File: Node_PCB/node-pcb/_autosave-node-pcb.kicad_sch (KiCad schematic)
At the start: 37 parts, among them J1 TYPE-C-31-M-12, J2 TSW-102-07-G-S, J3 TSW-118-07-L-D, J4 TSW-118-07-L-D, U1 NCP1117ST33T3G, U3 RP2040, U4 W25Q32JVSSIQ, X1 12MHz

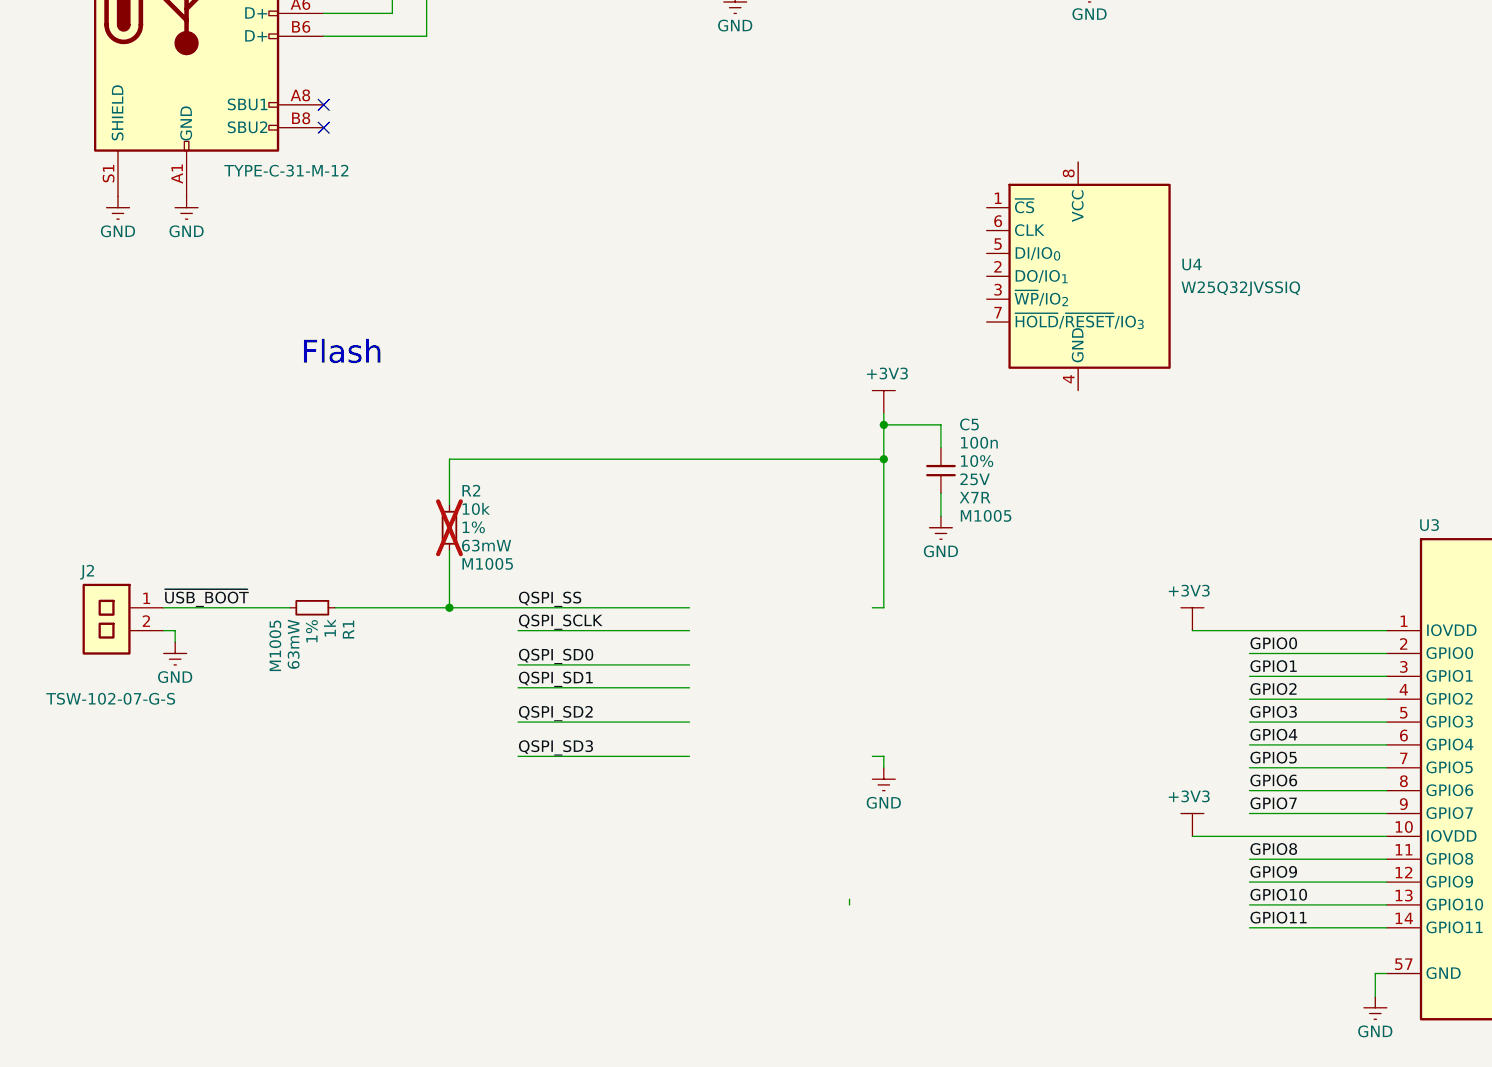
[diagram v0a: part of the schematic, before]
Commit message: Add new images for documentation and update existing schematic
- Added minimal example flash image to the documentation.
- Added schematic flash image to the documentation.
- Updated existing schematic power image.
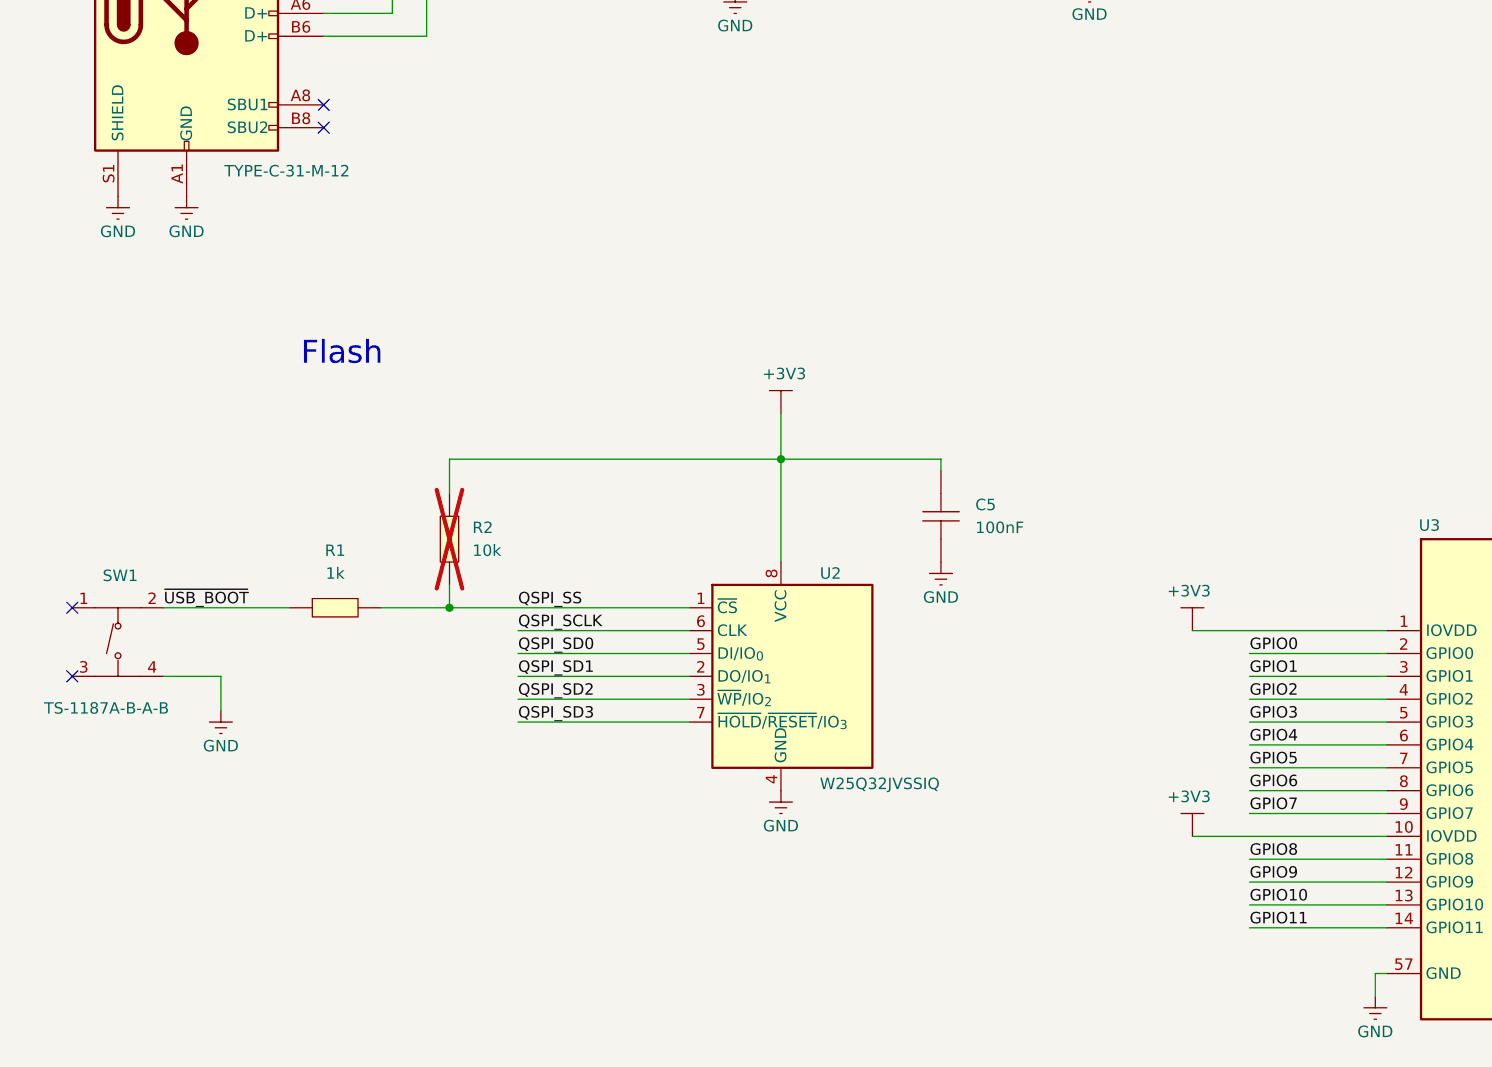
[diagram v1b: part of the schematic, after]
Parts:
- removed C5: 100n, RPI_COMPILED:generic_capc1005x50, symbol RPI_DB:Capacitors | MLCC | M1005/RP-01BJ9Y-KRGF41
- removed J2: TSW-102-07-G-S, RPI_COMPILED:samtec_tsw-102-07-g-s, symbol RPI_DB:Connectors | Pin_Headers/RP-01JV5X-LY21H5
- removed R1: 1k, RPI_COMPILED:generic_resc1005x35, symbol RPI_DB:Resistors | Chip | M1005/RP-019A1P-4Z6ZWY
- removed R2: 10k, RPI_COMPILED:generic_resc1005x35, symbol RPI_DB:Resistors | Chip | M1005/RP-019A1P-53DHSX
- added C5: 100nF, EasyEDA:C0402, symbol EasyEDA:CL05B104KO5NNNC
- added R1: 1k, EasyEDA:R0402, symbol EasyEDA:0402WGF1001TCE
- added R2: 10k, EasyEDA:R0402, symbol EasyEDA:0402WGF1002TCE
- added SW1: TS-1187A-B-A-B, EasyEDA:SW-SMD_4P-L5.1-W5.1-P3.70-LS6.5-TL_H1.5, symbol EasyEDA:TS-1187A-B-A-B
- renumbered U4 to U2
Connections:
- net +3V3: now also U2.8 (VCC), C5.1, R2.1
- net GND: now also U2.4 (GND), C5.2, SW1.4 (D)
- net QSPI_SCLK: now also U2.6 (CLK)
- net QSPI_SD0: now also U2.5 (DI/IO_{0})
- net QSPI_SD1: now also U2.2 (DO/IO_{1})
- net QSPI_SD2: now also U2.3 (~{WP}/IO_{2})
- net QSPI_SD3: now also U2.7 (~{HOLD}/~{RESET}/IO_{3})
- net QSPI_SS: now also U2.1 (~{CS}), R1.2, R2.2
- net ~{USB_BOOT}: now also R1.1, SW1.2 (B)
- no-connect marks 2 -> 4
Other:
- moved on the sheet: U2
